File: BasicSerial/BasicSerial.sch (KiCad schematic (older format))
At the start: 19 parts, among them CN1 DB9_Male, J1 COM_SELECT, J2 IRQ_SELECT, J3 Bus_ISA_8bit, U1 16550, U2 1.8432 MHz, U3 74LS688 or GAL16V8, U4 GD75232N, Y1 1.8432 MHz

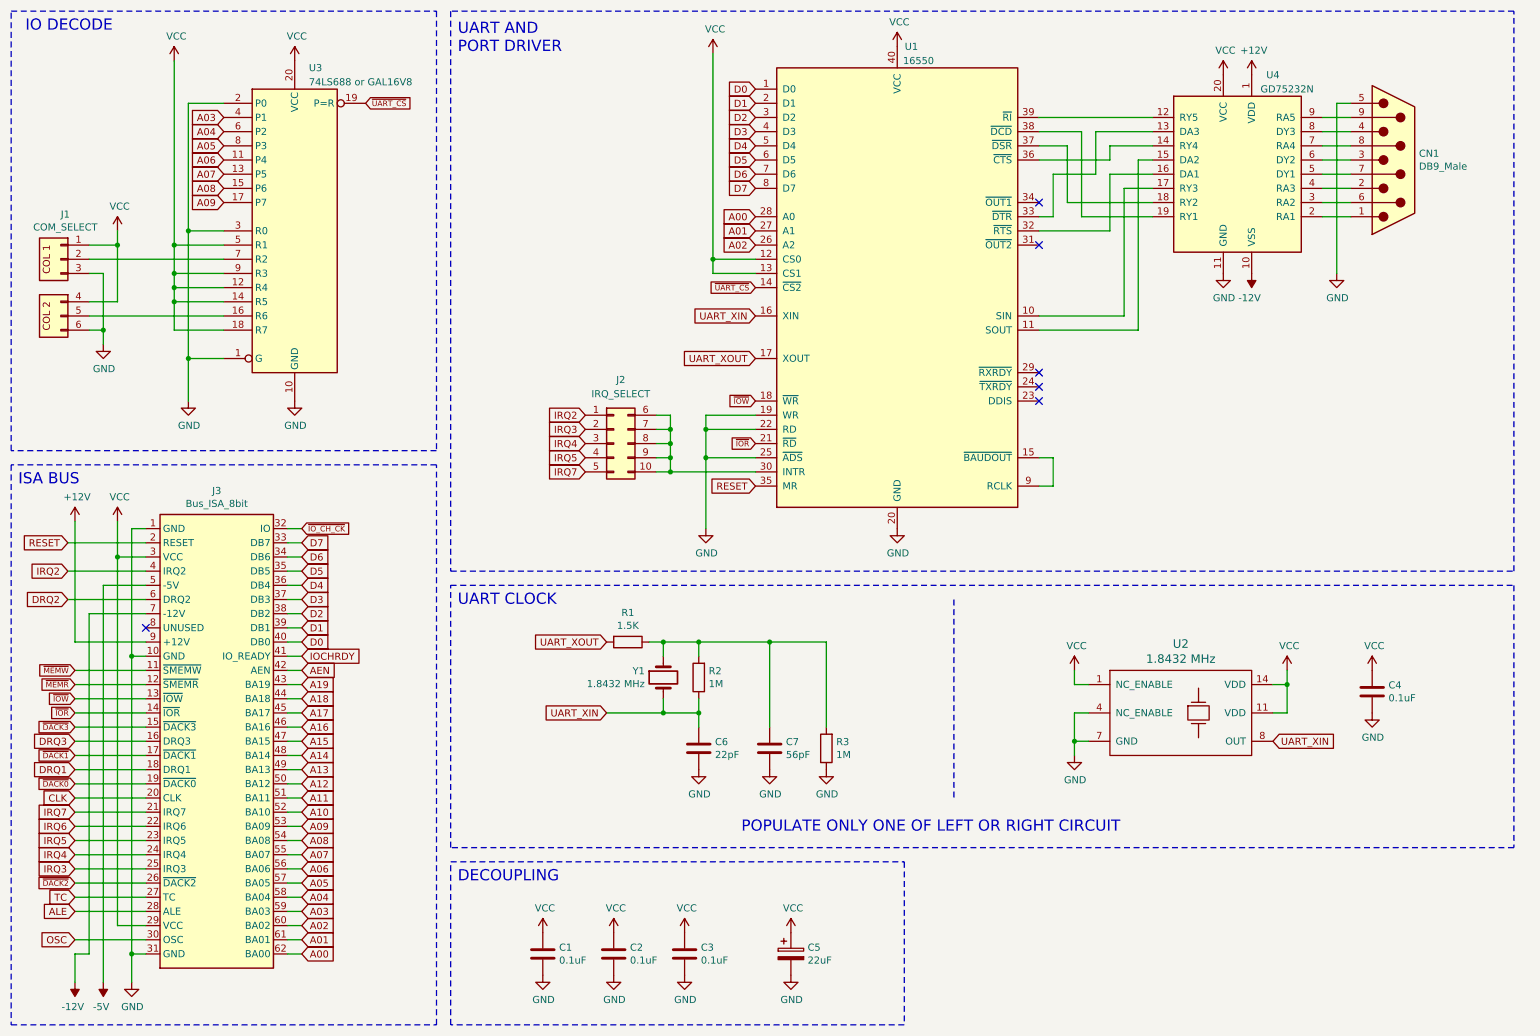
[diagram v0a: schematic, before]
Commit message: BasicSerial: Fix ERC issues, include AEN in IO addr decode, assign footprints.
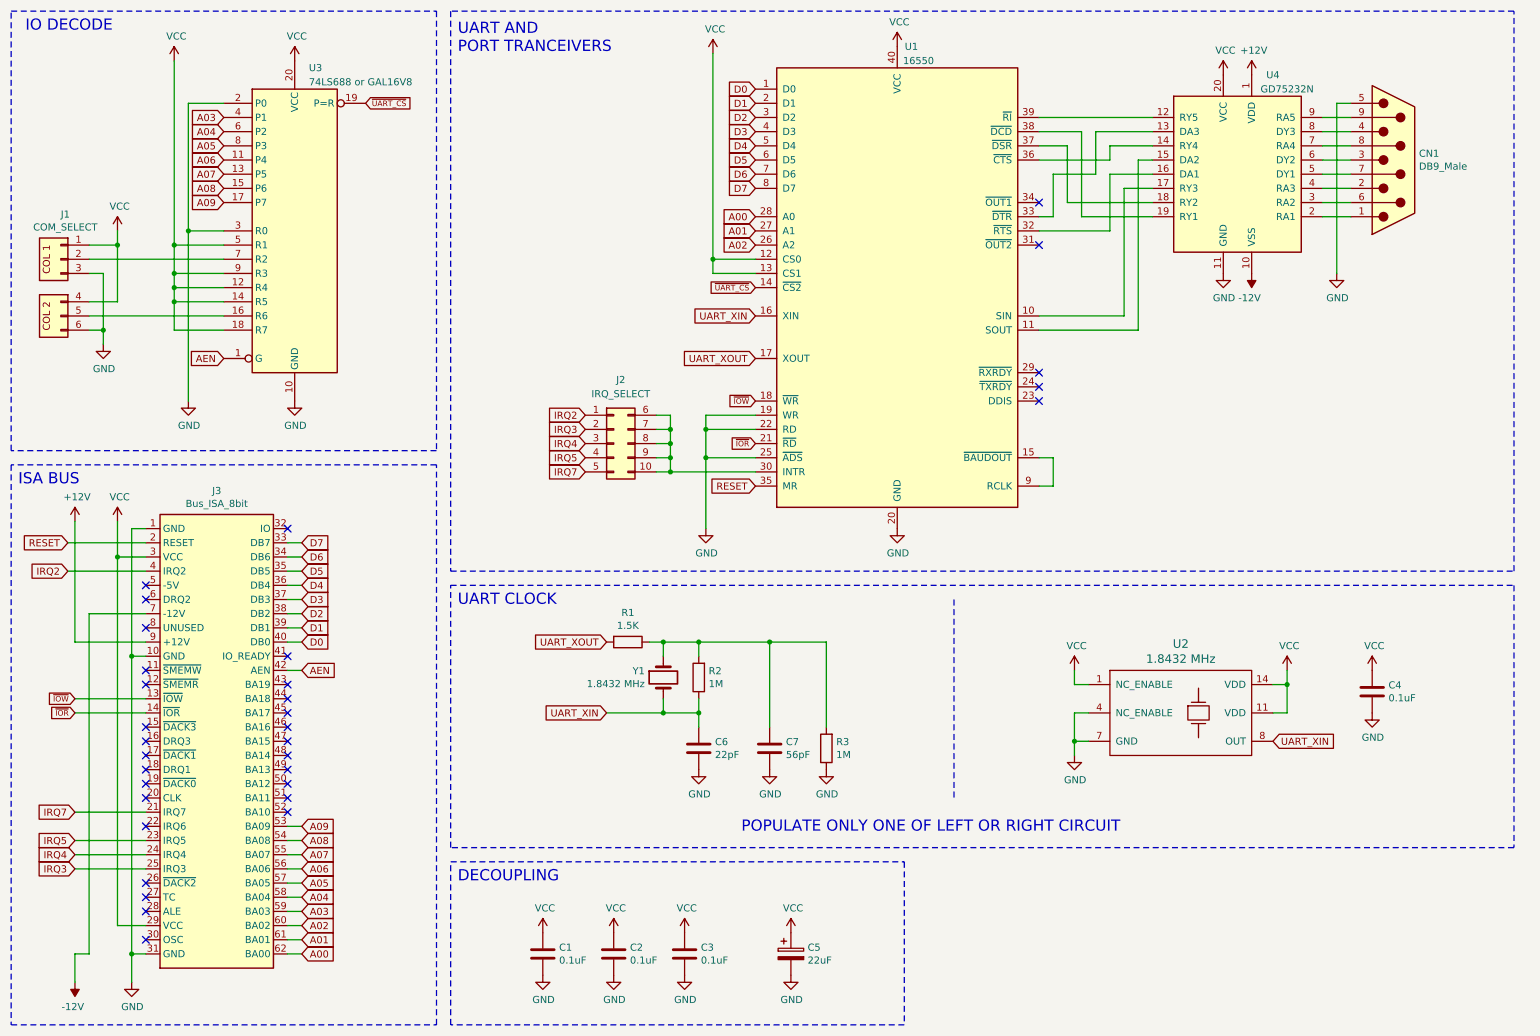
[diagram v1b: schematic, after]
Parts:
- C1, C2, C3, C4: footprint (none) -> Capacitor_THT:C_Disc_D5.1mm_W3.2mm_P5.00mm
- C5: footprint (none) -> Capacitor_THT:CP_Radial_D7.5mm_P2.50mm
- C6, C7: footprint (none) -> Capacitor_THT:C_Disc_D5.0mm_W2.5mm_P5.00mm
- CN1: footprint (none) -> Connector_Dsub:DSUB-9_Male_Horizontal_P2.77x2.54mm_EdgePinOffset9.40mm
- J1: footprint (none) -> 00Custom:PinHeader_3x02_P2.54mm_Vertical
- J2: footprint (none) -> Connector_PinHeader_2.54mm:PinHeader_2x05_P2.54mm_Vertical
- R1, R2, R3: footprint (none) -> Resistor_THT:R_Axial_DIN0207_L6.3mm_D2.5mm_P10.16mm_Horizontal
- U1: footprint Package_DIP:DIP-40_W15.24mm -> Package_DIP:DIP-40_W15.24mm_Socket
- U2: footprint (none) -> 00Custom:Crystal_DIP8_DIP14
- U3: footprint (none) -> Package_DIP:DIP-20_W7.62mm_Socket
- U4: footprint Package_DIP:DIP-20_W7.62mm -> Package_DIP:DIP-20_W7.62mm_Socket
- Y1: footprint (none) -> Crystal:Crystal_HC49-U_Horizontal
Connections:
- net AEN: now also U3.1 (G)
- net GND: no longer U3.1 (G)
- net -5V: no longer names the net of J3.5 (-5V)
- net A10: no longer names the net of J3.52 (BA10)
- net A11: no longer names the net of J3.51 (BA11)
- net A12: no longer names the net of J3.50 (BA12)
- net A13: no longer names the net of J3.49 (BA13)
- net A14: no longer names the net of J3.48 (BA14)
- net A15: no longer names the net of J3.47 (BA15)
- net A16: no longer names the net of J3.46 (BA16)
- net A17: no longer names the net of J3.45 (BA17)
- net A18: no longer names the net of J3.44 (BA18)
- net A19: no longer names the net of J3.43 (BA19)
- net ALE: no longer names the net of J3.28 (ALE)
- net CLK: no longer names the net of J3.20 (CLK)
- net DRQ1: no longer names the net of J3.18 (DRQ1)
- net DRQ2: no longer names the net of J3.6 (DRQ2)
- net DRQ3: no longer names the net of J3.16 (DRQ3)
- net IOCHRDY: no longer names the net of J3.41 (IO_READY)
- net IRQ6: no longer names the net of J3.22 (IRQ6)
- net OSC: no longer names the net of J3.30 (OSC)
- net TC: no longer names the net of J3.27 (TC)
- net ~DACK0: no longer names the net of J3.19 (~DACK0)
- net ~DACK1: no longer names the net of J3.17 (~DACK1)
- net ~DACK2: no longer names the net of J3.26 (~DACK2)
- net ~DACK3: no longer names the net of J3.15 (~DACK3)
- net ~IO_CH_CK: no longer names the net of J3.32 (IO)
- net ~MEMR: no longer names the net of J3.12 (~SMEMR)
- net ~MEMW: no longer names the net of J3.11 (~SMEMW)
- no-connect marks 6 -> 33
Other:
- note added: "UART AND\nPORT TRANCEIVERS"
- note removed: "UART AND\nPORT DRIVER"

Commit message: BasicSerial: Place DB-9 connector.
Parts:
- CN1: footprint Connector_Dsub:DSUB-9_Male_Horizontal_P2.77x2.54mm_EdgePinOffset9.40mm -> w_conn_d-sub:DB_9M
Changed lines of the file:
@@
 F 0 "CN1" H 10480 1646 50  0000 L CNN
 F 1 "DB9_Male" H 10480 1555 50  0000 L CNN
-F 2 "Connector_Dsub:DSUB-9_Male_Horizontal_P2.77x2.54mm_EdgePinOffset9.40mm" H 10300 1600 50  0001 C CNN
+F 2 "w_conn_d-sub:DB_9M" H 10300 1600 50  0001 C CNN
 F 3 " ~" H 10300 1600 50  0001 C CNN
 	1    10300 1600

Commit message: BasicSerial: Initial layout work.
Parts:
- renumbered U3 to U2, U4 to U3, U2 to U4
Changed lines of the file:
@@
 $EndComp
 $Comp
-L Interface_UART:GD75232N U4
+L Interface_UART:GD75232N U3
 U 1 1 60787022
 P 9200 1700
-F 0 "U4" H 9450 2400 50  0000 C CNN
+F 0 "U3" H 9450 2400 50  0000 C CNN
 F 1 "GD75232N" H 9550 2300 50  0000 C CNN
 F 2 "Package_DIP:DIP-20_W7.62mm_Socket" H 9200 900 50  0001 C CIN
@@
 	5500 2300 5500 850
 $Comp
-L 00Common:CRYSTAL_OSCILLATOR_BOTH_SIZES U2
+L 00Common:CRYSTAL_OSCILLATOR_BOTH_SIZES U4
 U 1 1 607DFD4C
 P 8800 5500
-F 0 "U2" H 8800 5987 60  0000 C CNN
+F 0 "U4" H 8800 5987 60  0000 C CNN
 F 1 "1.8432 MHz" H 8800 5881 60  0000 C CNN
 F 2 "00Custom:Crystal_DIP8_DIP14" H 8300 5500 60  0001 C CNN
@@
 Connection ~ 5200 3700
 $Comp
-L 74xx:74LS688 U3
+L 74xx:74LS688 U2
 U 1 1 60925648
 P 2550 2100
-F 0 "U3" H 2650 3250 50  0000 L CNN
+F 0 "U2" H 2650 3250 50  0000 L CNN
 F 1 "74LS688 or GAL16V8" H 2650 3150 50  0000 L CNN
 F 2 "Package_DIP:DIP-20_W7.62mm_Socket" H 2550 2100 50  0001 C CNN

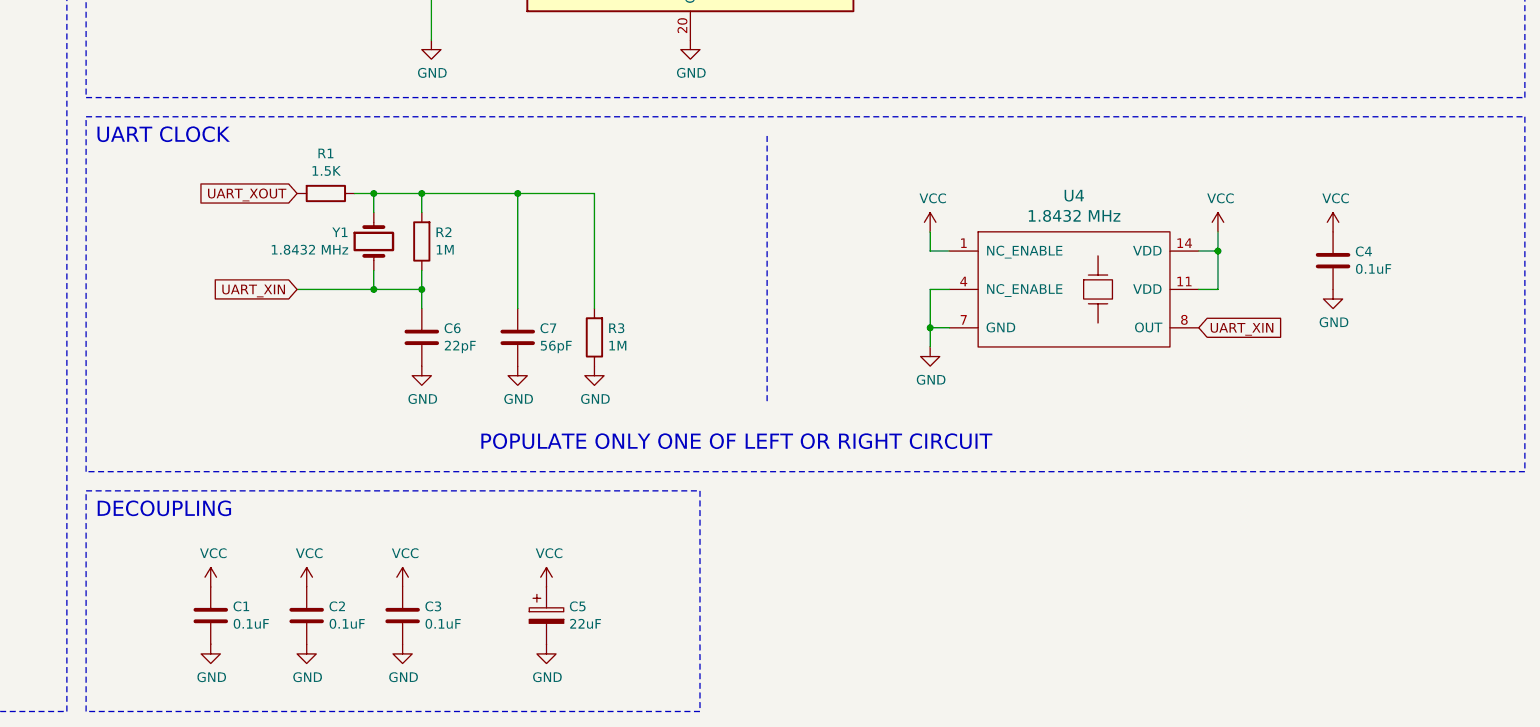
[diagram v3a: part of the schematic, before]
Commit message: BasicSerial: Remove discrete oscillator option, re-organize the IC layout.
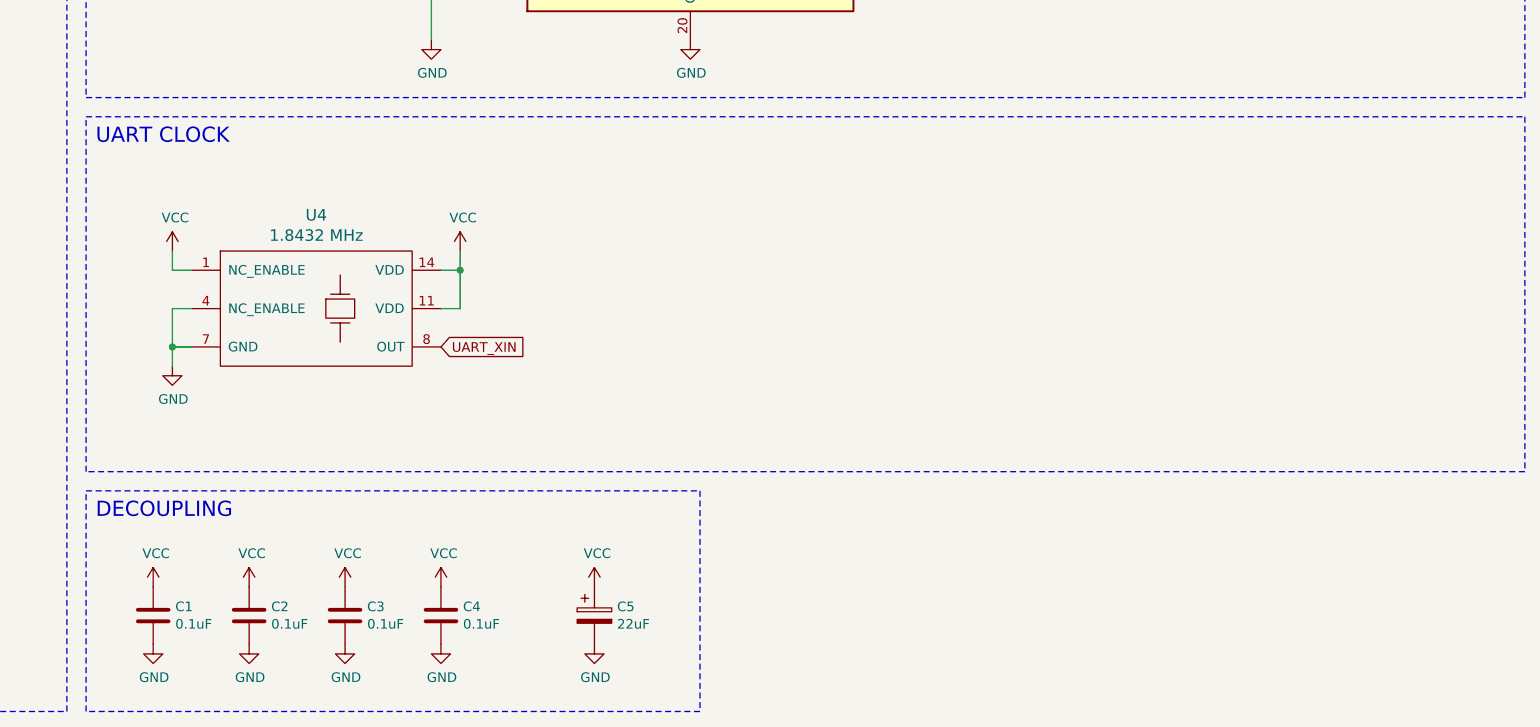
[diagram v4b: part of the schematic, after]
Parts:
- removed C6: 22pF, Capacitor_THT:C_Disc_D5.0mm_W2.5mm_P5.00mm, symbol Device:C
- removed C7: 56pF, Capacitor_THT:C_Disc_D5.0mm_W2.5mm_P5.00mm, symbol Device:C
- removed R1: 1.5K, Resistor_THT:R_Axial_DIN0207_L6.3mm_D2.5mm_P10.16mm_Horizontal, symbol Device:R
- removed R2, R3: 1M, Resistor_THT:R_Axial_DIN0207_L6.3mm_D2.5mm_P10.16mm_Horizontal, symbol Device:R
- removed Y1: 1.8432 MHz, Crystal:Crystal_HC49-U_Horizontal, symbol Device:Crystal
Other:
- note removed: "POPULATE ONLY ONE OF LEFT OR RIGHT CIRCUIT"
- moved on the sheet: C1, C2, C3, C4, C5, U4

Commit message: Basic Serial: Add +-12v decoupling caps. WIP on board routing.
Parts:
- added C6, C7: 4.7uF, Capacitor_THT:CP_Radial_D7.5mm_P2.50mm, symbol Device:CP
- J2: symbol Connector_Generic:Conn_02x05_Top_Bottom -> Connector_Generic:Conn_02x05_Odd_Even
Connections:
- net +12V: now also C6.1
- net -12V: now also C7.2
- net GND: now also C6.2, C7.1
- net IRQ3: now also J2.3 (Pin_3); no longer J2.2 (Pin_2)
- net IRQ4: now also J2.5 (Pin_5); no longer J2.3 (Pin_3)
- net IRQ5: now also J2.7 (Pin_7); no longer J2.4 (Pin_4)
- net IRQ7: now also J2.9 (Pin_9); no longer J2.5 (Pin_5)
- net at J2.10 (Pin_10), J2.6 (Pin_6), J2.8 (Pin_8)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: now also J2.2 (Pin_2), J2.4 (Pin_4); no longer J2.7 (Pin_7), J2.9 (Pin_9)
- net SER_PIN1: now reaches CN1.1, U3.2 (RA1)
- net SER_PIN6: now reaches CN1.6, U3.3 (RA2)
- net SER_PIN2: now reaches CN1.2, U3.4 (RA3)
- net SER_PIN7: now reaches CN1.7, U3.5 (DY1)
- net SER_PIN3: now reaches CN1.3, U3.6 (DY2)
- net SER_PIN8: now reaches CN1.8, U3.7 (RA4)
- net SER_PIN4: now reaches CN1.4, U3.8 (DY3)
- net SER_PIN9: now reaches CN1.9, U3.9 (RA5)
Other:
- moved on the sheet: C1, C2, C3, C4, C5, CN1

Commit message: First pass at PCB layout complete.
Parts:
- CN1: value DB9_Male -> DB9 Male
- U1: value 16550 -> 16550/16C550
- U2: value 74LS688 or GAL16V8 -> 74LS688, 74HCT688 or GAL16V8
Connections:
- net GND: no longer U4.4 (NC_ENABLE)
- net VCC: now also U4.4 (NC_ENABLE)
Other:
- moved on the sheet: CN1, J2, U1, U3
